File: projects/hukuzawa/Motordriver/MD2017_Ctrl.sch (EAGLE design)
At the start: 18 parts, among them IC1 PIC16F648, J1 3X2A, Q1 CERALOCK

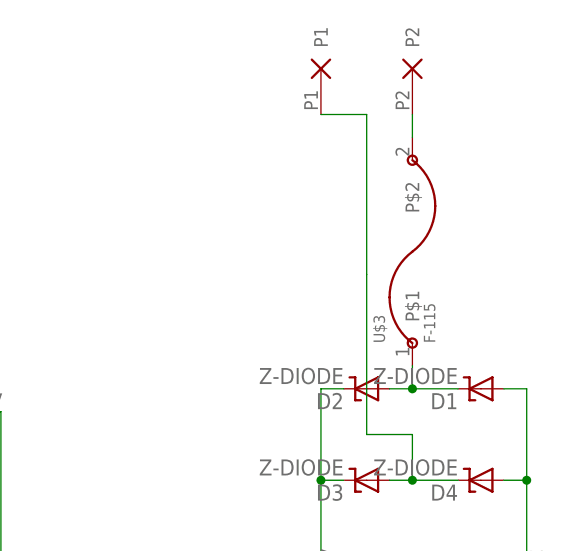
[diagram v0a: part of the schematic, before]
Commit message: モータードライバ修正
使用ヒューズホルダー変更
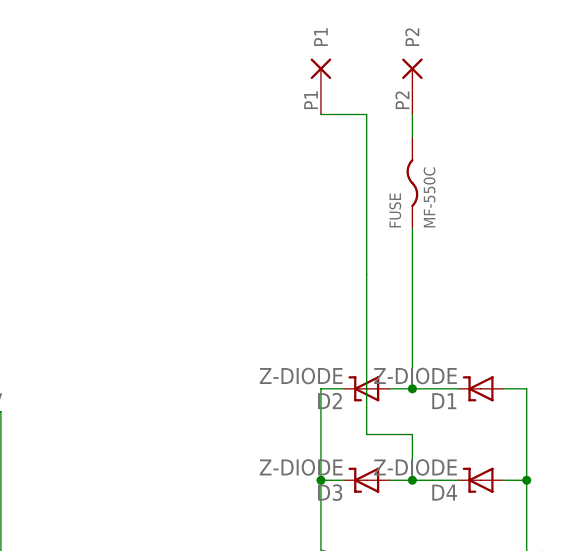
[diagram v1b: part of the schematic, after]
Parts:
- removed U$3: F-115, testLib:F-115
- added FUSE: MF-550C, MF5xx:MF-550C
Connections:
- removed net NBATT1: D1.C, D2.A, U$3.P$1
- new net N$1: D1.C, D2.A, FUSE.PA
- net BATTA: now also FUSE.PB; no longer U$3.P$2
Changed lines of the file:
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@@
 <part name="R1" library="rcl" deviceset="R-US_" device="R3216W" value="1k"/>
 <part name="U$2" library="Powerio" deviceset="2P" device=""/>
-<part name="U$3" library="testLib" deviceset="F-115" device=""/>
 <part name="C1" library="FP-21T for MITS" deviceset="CPOL-EU2" device="-5MM" value="47uF"/>
 <part name="C2" library="FP-21T for MITS" deviceset="CPOL-EU2" device="-5MM" value="47uF"/>
@@
 <part name="D3" library="diode" deviceset="Z-DIODE" device=""/>
 <part name="D4" library="diode" deviceset="Z-DIODE" device=""/>
+<part name="FUSE" library="MF5xx" deviceset="MF-5" device="50C"/>
 </parts>
 <sheets>
@@
 <instance part="R1" gate="G$1" x="-50.8" y="27.94" rot="R90"/>
 <instance part="U$2" gate="G1" x="63.5" y="53.34"/>
-<instance part="U$3" gate="G$1" x="68.58" y="33.02" rot="R90"/>
 <instance part="C1" gate="G$1" x="-63.5" y="43.18"/>
 <instance part="C2" gate="G$1" x="-58.42" y="43.18"/>
@@
 <instance part="D3" gate="1" x="63.5" y="7.62" rot="R180"/>
 <instance part="D4" gate="1" x="76.2" y="7.62" rot="R180"/>
+<instance part="FUSE" gate="FUSE" x="68.58" y="40.64" rot="R90"/>
 </instances>
 <busses>
@@
 </segment>
 </net>
-<net name="NBATT1" class="0">
-<segment>
-<wire x1="73.66" y1="17.78" x2="68.58" y2="17.78" width="0.1524" layer="91"/>
-<wire x1="68.58" y1="17.78" x2="66.04" y2="17.78" width="0.1524" layer="91"/>
-<wire x1="68.58" y1="17.78" x2="68.58" y2="20.32" width="0.1524" layer="91"/>
-<junction x="68.58" y="17.78"/>
-<pinref part="U$3" gate="G$1" pin="P$1"/>
-<pinref part="D1" gate="1" pin="C"/>
-<pinref part="D2" gate="1" pin="A"/>
-</segment>
-</net>
 <net name="BATTB" class="0">
 <segment>
@@
 <net name="BATTA" class="0">
 <segment>
-<pinref part="U$3" gate="G$1" pin="P$2"/>
 <pinref part="U$2" gate="G1" pin="P2"/>
 <wire x1="68.58" y1="45.72" x2="68.58" y2="48.26" width="0.1524" layer="91"/>
-</segment>
-</net>
+<pinref part="FUSE" gate="FUSE" pin="PB"/>
+</segment>
+</net>
+<net name="N$1" class="0">
+<segment>
+<pinref part="D1" gate="1" pin="C"/>
+<wire x1="73.66" y1="17.78" x2="68.58" y2="17.78" width="0.1524" layer="91"/>
+<wire x1="68.58" y1="17.78" x2="66.04" y2="17.78" width="0.1524" layer="91"/>
+<pinref part="D2" gate="1" pin="A"/>
+<pinref part="FUSE" gate="FUSE" pin="PA"/>
+<wire x1="68.58" y1="35.56" x2="68.58" y2="17.78" width="0.1524" layer="91"/>
+<junction x="68.58" y="17.78"/>
+</segment>
+</net>
